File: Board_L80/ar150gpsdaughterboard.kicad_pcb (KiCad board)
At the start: 2 copper layers, 30.5 x 19.2 mm, 9 parts, among them P1 CONN_02X05, Q1 BSS138, U1 QUECTEL-L80

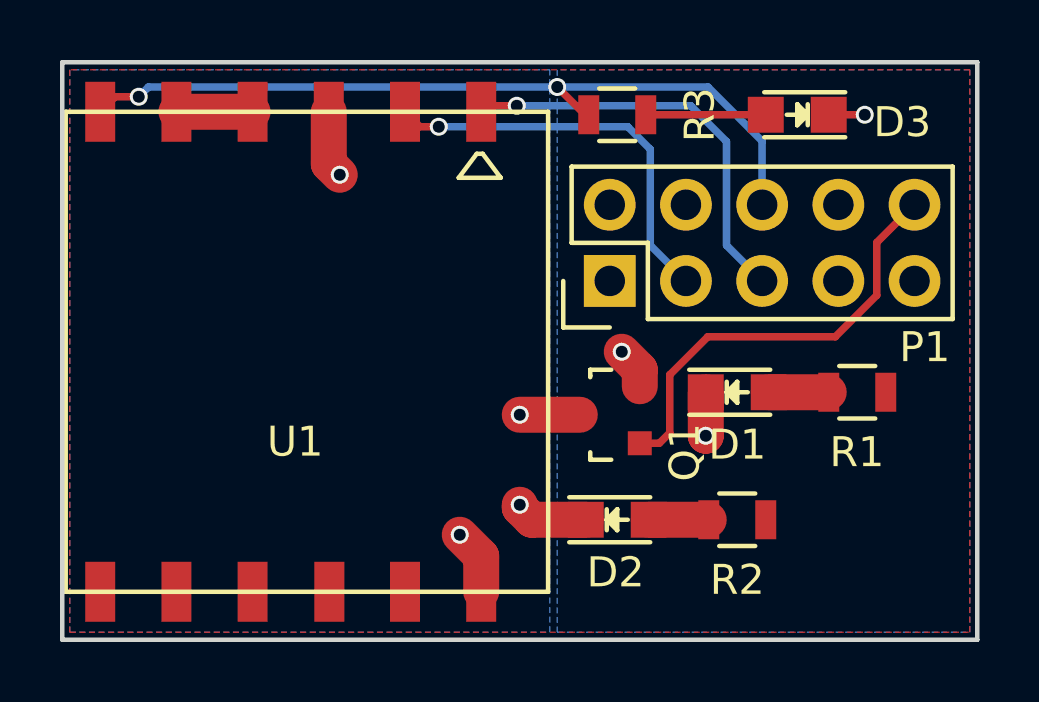
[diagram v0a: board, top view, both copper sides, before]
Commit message: updated baord for L80 - should sit more correclty now
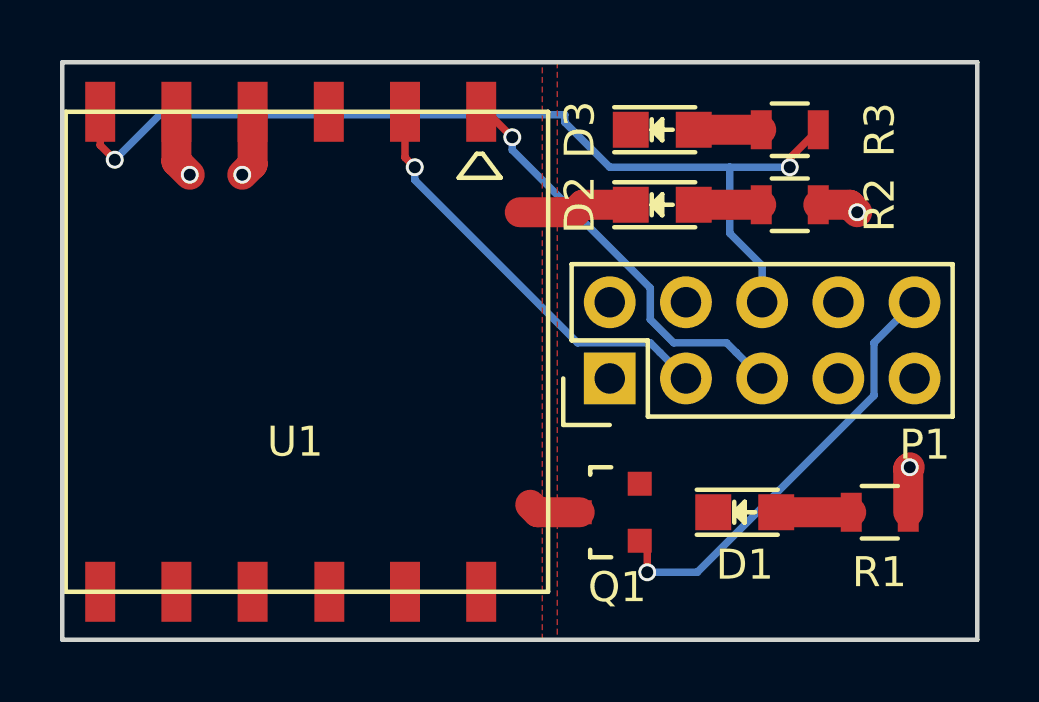
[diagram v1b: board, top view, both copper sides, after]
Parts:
- moved R2 10.6 mm to (143.0, 100.0)
- moved D2 10.6 mm to (138.8, 100.0)
- moved R3 5.77 mm to (143.0, 97.5), turned to 180 degrees
- moved D3 4.53 mm to (138.8, 97.5), turned to 0 degrees
- moved R1 4.07 mm to (146.0, 110.2)
- moved D1 4.01 mm to (141.5, 110.2)
- moved Q1 3.25 mm to (137.0, 110.2)
- moved P1 3.25 mm to (137.0, 105.8)
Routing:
- net GP_14: track 26.7 -> 32.4 mm
- net +3V3: track 2.54 -> 7.45 mm, vias 0 -> 4
- net GND: track 4.05 -> 0.00 mm, vias 3 -> 0
- net GP_GND: track 8.91 -> 5.56 mm, vias 4 -> 0
- net Net-(D3-Pad2): track 4.00 -> 2.25 mm
- net RX: track 13.6 -> 14.2 mm
- net Net-(D1-Pad2): track 2.00 -> 2.50 mm
- net GP_17: track 14.6 -> 14.8 mm, vias 0 -> 1
- added copper zone on B.Cu, net +3V3
- added copper zone on F.Cu, net GND
- added copper zone on F.Cu, net GP_GND
- removed copper zone on F.Cu, net +3V3
- removed copper zone on B.Cu, net GND
- removed copper zone on B.Cu, net GP_GND
